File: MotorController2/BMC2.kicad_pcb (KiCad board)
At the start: 2 copper layers, 142.2 x 57.2 mm, 132 parts, among them P1 Sensor, P10 GND, P11 I2C, P12 CAN, P2 CAN, P3 DATA, P4 USB_OTG, P5 PhaseA, P6 PhaseB, P7 PhaseC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

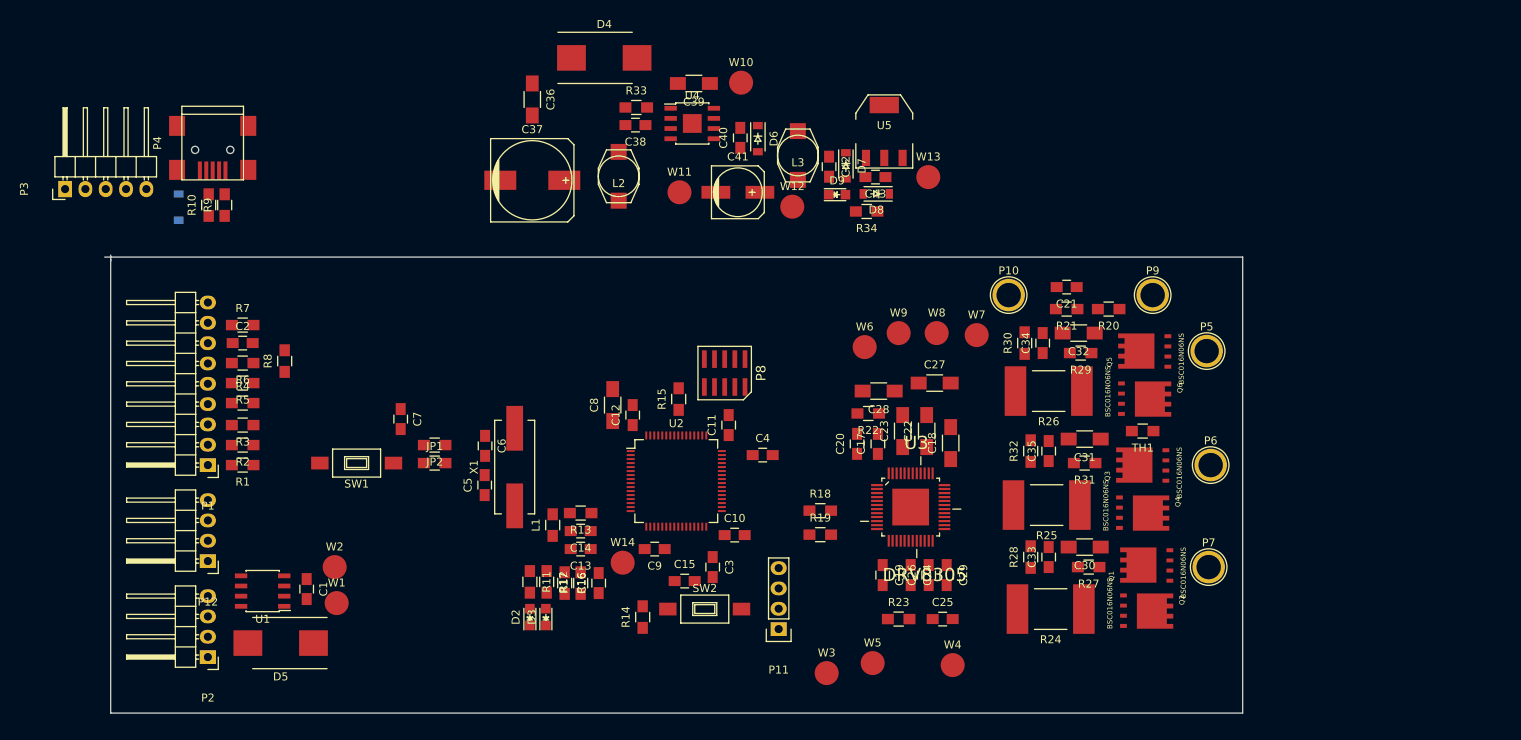
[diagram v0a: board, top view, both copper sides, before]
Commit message: Laying out power section.
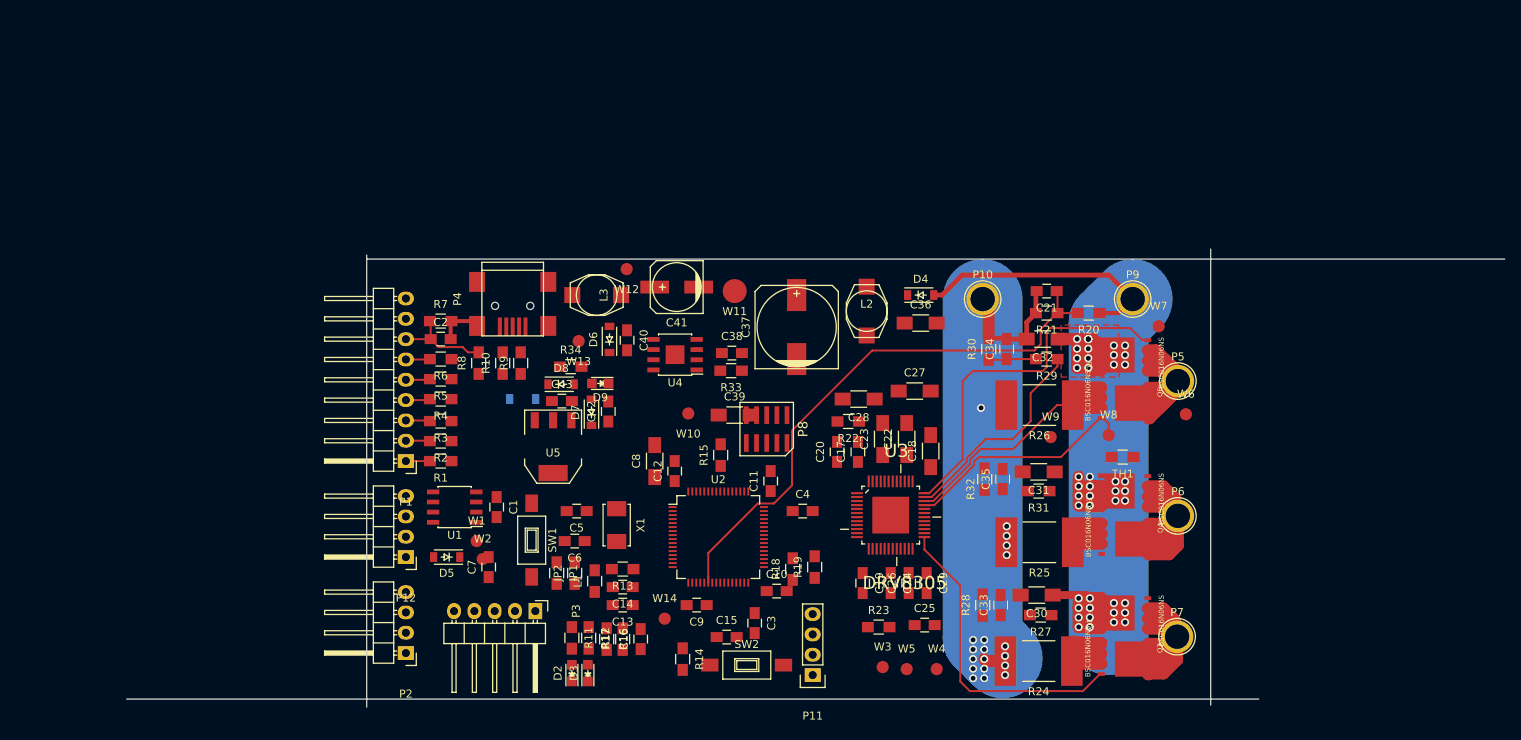
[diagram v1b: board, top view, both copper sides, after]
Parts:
- D4, D5: value D -> 60V 2A; footprint Diodes_SMD:DO-214AB_Handsoldering -> Diodes_SMD:SOD-123
- Q1, Q2, Q3, Q4, Q5, Q6: footprint SON127P532X615X110-8N:SON127P532X615X110-8N -> Local:SON127P532X615X110-8N
- W1, W10, W12, W13, W14, W2, W3, W4, W5, W6, W7, W8, W9: footprint Measurement_Points:Measurement_Point_Round-SMD-Pad_Big -> Measurement_Points:Measurement_Point_Round-SMD-Pad_Small
- X1: footprint Crystals:Crystal_HC49-SD_SMD -> Crystals:ABM3
- moved P3 79.0 mm to (141.1, 99.0), turned to 270 degrees
- moved U5 57.2 mm to (143.3, 78.5), turned to 180 degrees
- moved C36 56.0 mm to (189.2, 63.0), turned to 0 degrees
- moved D4 49.4 mm to (189.2, 59.5)
- moved D1 49.2 mm to (139.5, 72.5), turned to 180 degrees
- moved W13 48.3 mm to (146.5, 65.2), turned to 180 degrees
- moved C43 48.2 mm to (144.4, 72.8), turned to 0 degrees
- moved D8 46.0 mm to (144.3, 70.7), turned to 0 degrees
- moved D7 44.3 mm to (148.1, 74.2), turned to 90 degrees
- moved P4 42.3 mm to (138.2, 60.0)
- moved R9 41.9 mm to (139.2, 68.0)
- moved W10 41.9 mm to (160.2, 74.3), turned to 180 degrees
- moved R34 41.8 mm to (145.5, 68.5), turned to 0 degrees
- moved C39 41.8 mm to (166.0, 74.5), turned to 0 degrees
- moved R10 41.7 mm to (137.0, 68.0)
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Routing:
- net +36V: track 0.00 -> 128.3 mm, vias 0 -> 44
- net GND: track 0.00 -> 76.8 mm, vias 0 -> 19
- net /Controller/VSenseSupply: track 0.00 -> 70.2 mm
- net /power/PhaseA: track 0.00 -> 68.3 mm
- net Net-(Q5-Pad4): track 0.00 -> 45.5 mm
- net Net-(Q2-Pad4): track 0.00 -> 38.9 mm
- net /power/PhaseB: track 0.00 -> 38.8 mm
- net Net-(C29-Pad1): track 0.00 -> 38.5 mm
- net /power/PhaseC: track 0.00 -> 36.7 mm
- net Net-(Q6-Pad4): track 0.00 -> 29.5 mm
- net Net-(C24-Pad1): track 0.00 -> 18.5 mm
- net Net-(C26-Pad1): track 0.00 -> 14.0 mm
- net Net-(C2-Pad1): track 0.00 -> 12.1 mm
- net /Controller/VSenseA: track 0.00 -> 5.69 mm
- net Net-(P1-Pad4): track 0.00 -> 3.05 mm
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- added copper zone on F.Cu, net +36V
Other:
- board size 142.2 x 57.2 mm -> 172.2 x 57.2 mm
- net class Drive added: clearance 0.2, trace_width 0.3, via_dia 0.6, via_drill 0.4
- net class High Power added: clearance 0.2, trace_width 0.25, via_dia 1, via_drill 0.6
- net class Low Power added: clearance 0.2, trace_width 0.5, via_dia 0.6, via_drill 0.4

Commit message: More of the layout done.
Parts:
- removed W6: SHA, Measurement_Points:Measurement_Point_Round-SMD-Pad_Small
- removed W9: SLA, Measurement_Points:Measurement_Point_Round-SMD-Pad_Small
- R24, R25, R26: footprint Local:R_PSR400 -> Local:R_PSR400_SENSE
- moved R7 42.4 mm to (138.1, 104.2)
- moved C2 42.4 mm to (138.0, 106.5)
- moved R8 39.9 mm to (142.5, 107.0), turned to 270 degrees
- moved C7 37.5 mm to (165.2, 71.0), turned to 180 degrees
- moved R6 35.6 mm to (138.1, 102.0)
- moved R5 31.1 mm to (138.2, 99.8)
- moved JP1 28.5 mm to (164.2, 74.5)
- moved JP2 28.5 mm to (166.5, 74.5)
- moved R4 26.3 mm to (138.1, 97.2)
- moved P1 25.8 mm to (133.5, 104.6)
- moved P2 25.4 mm to (133.5, 80.3)
- moved P12 25.0 mm to (133.5, 68.8)
- moved W13 23.5 mm to (137.5, 87.0)
- moved R3 21.4 mm to (138.0, 94.8)
- moved W11 19.9 mm to (185.8, 57.0)
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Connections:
- C24 pad 2: GND -> Net-(C24-Pad2)
- C26 pad 2: GND -> Net-(C26-Pad2)
- C29 pad 2: GND -> Net-(C29-Pad2)
- P1 pad 1: Net-(P1-Pad1) -> Net-(C2-Pad1)
- P1 pad 7: Net-(C2-Pad1) -> Net-(P1-Pad7)
- Q2 pad 1: Net-(C24-Pad1) -> Net-(Q2-Pad1)
- Q2 pad 2: Net-(C24-Pad1) -> Net-(Q2-Pad1)
- Q2 pad 3: Net-(C24-Pad1) -> Net-(Q2-Pad1)
- Q4 pad 1: Net-(C26-Pad1) -> Net-(Q4-Pad1)
- Q4 pad 2: Net-(C26-Pad1) -> Net-(Q4-Pad1)
- Q4 pad 3: Net-(C26-Pad1) -> Net-(Q4-Pad1)
- Q6 pad 1: Net-(C29-Pad1) -> Net-(Q6-Pad1)
- Q6 pad 2: Net-(C29-Pad1) -> Net-(Q6-Pad1)
- Q6 pad 3: Net-(C29-Pad1) -> Net-(Q6-Pad1)
- R1 pad 1: /Controller/EndStop1 -> /Controller/Index
- R1 pad 2: Net-(P1-Pad1) -> Net-(P1-Pad7)
- R2 pad 2: Net-(P1-Pad2) -> Net-(P1-Pad6)
- R24 pad 1: Net-(C24-Pad1) -> Net-(Q2-Pad1)
- R24 pad 2: GND -> Net-(C24-Pad1)
- R25 pad 1: Net-(C26-Pad1) -> Net-(Q4-Pad1)
- R25 pad 2: GND -> Net-(C26-Pad1)
- R26 pad 1: Net-(C29-Pad1) -> Net-(Q6-Pad1)
- R26 pad 2: GND -> Net-(C29-Pad1)
- R3 pad 1: /Controller/Index -> /Controller/EndStop1
- R3 pad 2: Net-(P1-Pad3) -> Net-(P1-Pad5)
- R5 pad 2: Net-(P1-Pad5) -> Net-(P1-Pad3)
- R6 pad 2: Net-(P1-Pad6) -> Net-(P1-Pad2)
- U2 pad 34: /Controller/INLA -> /Controller/INLC
- U2 pad 36: /Controller/INLC -> /Controller/INLA
- U2 pad 41: /Controller/INHA -> /Controller/INHC
- U2 pad 43: /Controller/INHC -> /Controller/INHA
- U3 pad 19: GND -> Net-(C24-Pad2)
- U3 pad 21: GND -> Net-(C26-Pad2)
- U3 pad 23: GND -> Net-(C29-Pad2)
- U3 pad 26: Net-(C24-Pad1) -> Net-(Q2-Pad1)
- U3 pad 31: Net-(C26-Pad1) -> Net-(Q4-Pad1)
- U3 pad 34: Net-(C29-Pad1) -> Net-(Q6-Pad1)
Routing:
- net GND: track 76.8 -> 298.7 mm, vias 19 -> 48
- net /Controller/TempDrv: track 0.00 -> 99.0 mm, vias 0 -> 2
- net /Controller/VSenseC: track 0.00 -> 83.0 mm, vias 0 -> 2
- net +36V: track 128.3 -> 204.3 mm, vias 44 -> 46
- net /Controller/VSenseB: track 0.00 -> 57.4 mm, vias 0 -> 2
- net Net-(C29-Pad2): track 0.00 -> 53.4 mm, vias 0 -> 2
- net Net-(Q2-Pad1): track 0.00 -> 50.2 mm
- net /power/PhaseC: track 36.7 -> 76.6 mm
- net Net-(Q6-Pad1): track 0.00 -> 38.5 mm
- net /power/PhaseB: track 38.8 -> 77.3 mm, vias 0 -> 2
- net Net-(Q3-Pad4): track 0.00 -> 37.0 mm
- net Net-(Q4-Pad1): track 0.00 -> 35.9 mm, vias 0 -> 2
- net Net-(C26-Pad2): track 0.00 -> 35.8 mm, vias 0 -> 2
- net Net-(Q1-Pad4): track 0.00 -> 32.3 mm
- net /Controller/VSenseA: track 5.69 -> 37.6 mm
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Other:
- board size 172.2 x 57.2 mm -> 178.2 x 57.8 mm

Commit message: More tweaks
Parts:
- moved C24 0.50 mm to (186.2, 95.6)
- moved R19 0.45 mm to (179.8, 92.8)
- moved C29 0.40 mm to (190.6, 93.1)
- moved C26 0.30 mm to (188.4, 95.1)
- moved C19 0.20 mm to (182.2, 94.6)
- moved R18 0.20 mm to (177.8, 92.8)
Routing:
- net Net-(C24-Pad2): track 29.0 -> 35.2 mm
- net Net-(C24-Pad1): track 31.7 -> 33.4 mm
- net Net-(C26-Pad1): track 34.8 -> 35.6 mm
- net Net-(C26-Pad2): track 35.8 -> 35.1 mm
- net Net-(C19-Pad1): track 5.19 -> 5.79 mm

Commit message: Layout nearly complete.
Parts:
- added C44: 0.1uf (6V min), Capacitors_SMD:C_0805_HandSoldering, F.Cu at (137.5, 83.5)
- D1: moved to F.Cu
- moved D5 53.4 mm to (186.5, 56.5)
- moved W11 43.0 mm to (186.2, 100.0)
- moved W7 26.5 mm to (193.5, 70.5)
- moved W10 16.5 mm to (166.5, 59.2)
- moved R33 14.9 mm to (152.8, 59.0), turned to 0 degrees
- moved D6 14.8 mm to (164.2, 57.8)
- moved L3 13.6 mm to (163.0, 68.5), turned to 0 degrees
- moved C38 12.9 mm to (152.8, 61.2), turned to 180 degrees
- moved W2 11.9 mm to (146.5, 83.5)
- moved C41 11.0 mm to (154.5, 66.2), turned to 0 degrees
- moved C40 10.9 mm to (164.2, 63.2), turned to 90 degrees
- moved U4 7.43 mm to (159.2, 59.5), turned to 0 degrees
- moved W12 5.13 mm to (160.8, 65.0), turned to 0 degrees
- moved SW1 4.09 mm to (146.4, 95.7), turned to 0 degrees
- moved JP1 3.65 mm to (164.2, 78.2), turned to 90 degrees
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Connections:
- U4 pad 9: (no net) -> GND
- U5 pad 4: (no net) -> +3V3
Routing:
- net GND: track 298.6 -> 685.9 mm, vias 48 -> 78
- net +3V3: track 27.0 -> 193.5 mm, vias 0 -> 7
- net +5V: track 0.00 -> 90.2 mm, vias 0 -> 2
- net +8V: track 0.00 -> 72.6 mm, vias 0 -> 1
- net NRST: track 2.15 -> 66.0 mm, vias 0 -> 4
- net /Controller/USB_DP: track 0.00 -> 56.6 mm, vias 0 -> 2
- net /Controller/USB_DM: track 0.00 -> 53.6 mm, vias 0 -> 2
- net Net-(C37-Pad1): track 0.00 -> 39.9 mm
- net /Controller/EndStop1: track 0.00 -> 36.4 mm, vias 0 -> 2
- net /Controller/EndStop2: track 0.00 -> 35.0 mm, vias 0 -> 2
- net /Controller/Index: track 0.00 -> 34.6 mm, vias 0 -> 2
- net +3.3VADC: track 12.3 -> 44.0 mm, vias 0 -> 2
- net /Controller/CAN_RX: track 0.00 -> 30.4 mm, vias 0 -> 2
- net /Controller/CAN_STBY: track 0.00 -> 30.2 mm, vias 0 -> 2
- net /Controller/UART_RX: track 0.00 -> 28.9 mm
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- added copper zone on B.Cu, net +36V
- added copper zone on F.Cu, net /power/PhaseA
- added copper zone on F.Cu, net /power/PhaseB
- added copper zone on F.Cu, net /power/PhaseC
- added copper zone on B.Cu, net GND
- added copper zone on F.Cu, net GND

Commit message: About to change via drill size.
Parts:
- moved W2 7.91 mm to (144.0, 76.0)
- moved R8 3.25 mm to (142.5, 103.8)
- moved W13 1.58 mm to (138.0, 85.5)
- moved W1 1.53 mm to (142.7, 83.2)
- moved C8 1.05 mm to (158.2, 79.2)
- moved D5 0.95 mm to (187.4, 56.8)
- moved C39 0.71 mm to (173.5, 69.8)
- moved X1 0.55 mm to (154.8, 86.2)
- moved SW2 0.55 mm to (170.2, 107.2)
- moved D2 0.50 mm to (159.8, 107.2)
- moved D3 0.50 mm to (162.0, 107.2)
- moved P4 0.50 mm to (141.2, 60.2)
- moved C5 0.41 mm to (151.4, 83.6)
- moved C6 0.40 mm to (151.4, 88.3)
- moved R10 0.35 mm to (136.8, 68.0)
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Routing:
- net GND: track 685.9 -> 719.0 mm, vias 78 -> 81
- net (no net): track 0.00 -> 10.2 mm, vias 1 -> 0
- net Net-(Q3-Pad4): track 36.6 -> 44.6 mm
- net Net-(C37-Pad1): track 39.9 -> 44.2 mm
- net /Controller/Temp: track 28.0 -> 24.2 mm
- net Net-(P4-Pad3): track 6.66 -> 9.73 mm
- net /Controller/CAN_RX: track 30.4 -> 32.8 mm
- net Net-(P12-Pad4): track 21.2 -> 23.1 mm
- net Net-(P4-Pad2): track 5.20 -> 7.12 mm
- net /power/PhaseB: track 94.8 -> 93.2 mm
- net Net-(C2-Pad1): track 12.9 -> 13.9 mm
- net +8V: track 72.6 -> 73.5 mm
- net /Controller/UART_TX: track 27.3 -> 26.4 mm
- net /Controller/USB_DM: track 53.6 -> 54.5 mm
- net /Controller/VSenseC: track 105.4 -> 104.6 mm
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- removed copper zone on F.Cu, net +36V
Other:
- board size 178.2 x 57.8 mm -> 96 x 56 mm
- net class Default: via_drill 0.4 -> 0.3
- net class Drive: via_drill 0.4 -> 0.3
- net class Low Power: via_drill 0.4 -> 0.3

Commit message: Nearly there.
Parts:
- moved R14 2.50 mm to (174.8, 100.1)
- moved C3 2.25 mm to (172.5, 100.0)
- moved C27 1.46 mm to (189.2, 72.8)
- moved W7 1.25 mm to (192.5, 69.8)
- moved C18 1.14 mm to (190.5, 78.0)
- moved R22 0.55 mm to (180.8, 75.3)
- moved C35 0.25 mm to (199.5, 82.2)
- moved R32 0.25 mm to (197.2, 82.2)
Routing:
- net GND: track 719.0 -> 707.8 mm, vias 81 -> 86
- net Net-(Q3-Pad4): track 44.6 -> 36.9 mm
- net /power/PhaseB: track 93.2 -> 99.1 mm
- net Net-(C3-Pad1): track 8.99 -> 5.75 mm
- net Net-(C15-Pad1): track 16.3 -> 19.0 mm
- net /Controller/MISO: track 17.2 -> 15.8 mm
- net Net-(Q5-Pad4): track 47.1 -> 48.4 mm
- net +36V: track 221.6 -> 222.7 mm
- net +3V3: track 193.9 -> 194.9 mm
- net Net-(C27-Pad1): track 13.4 -> 12.4 mm
- net /Controller/VSenseC: track 104.6 -> 105.5 mm
- net /Controller/VSenseSupply: track 70.9 -> 71.6 mm
- net +5V: track 90.1 -> 89.5 mm
- net Net-(Q4-Pad4): track 29.9 -> 30.4 mm

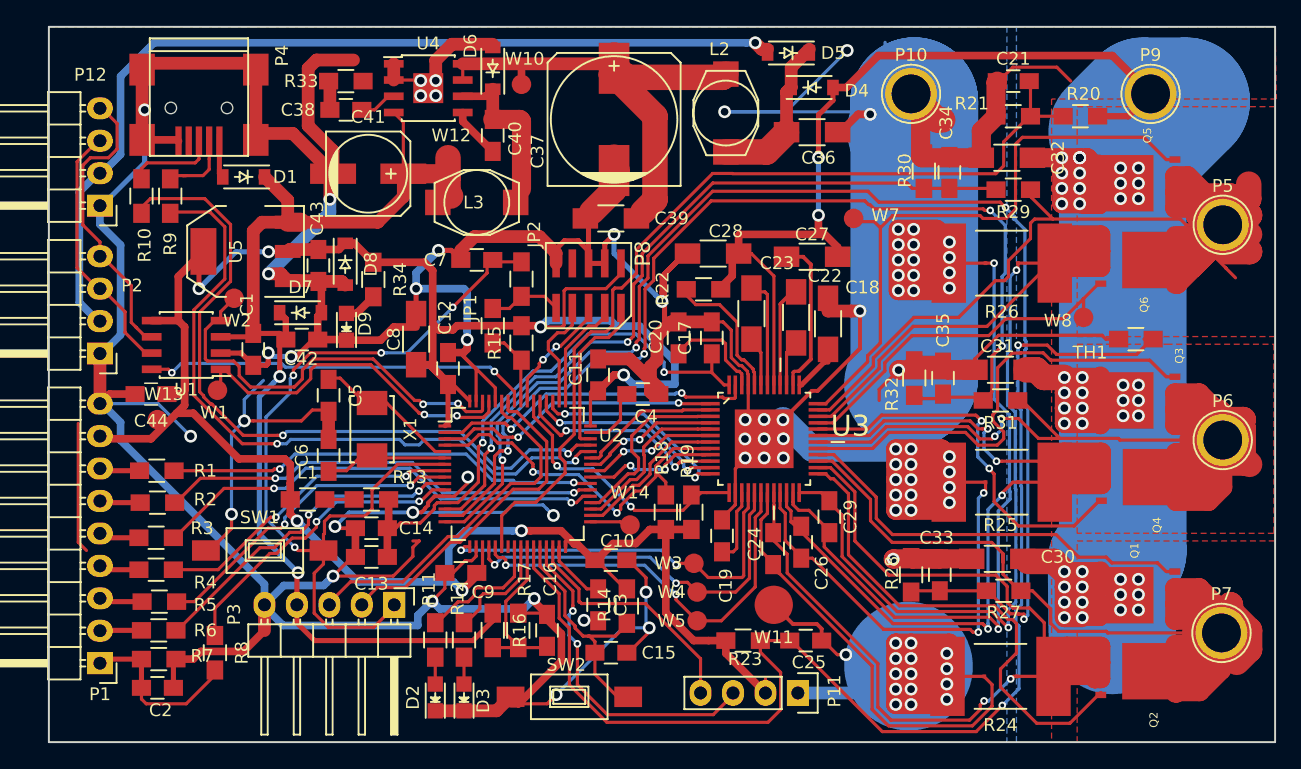
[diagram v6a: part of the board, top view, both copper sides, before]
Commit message: Fixes for soldermask clearences
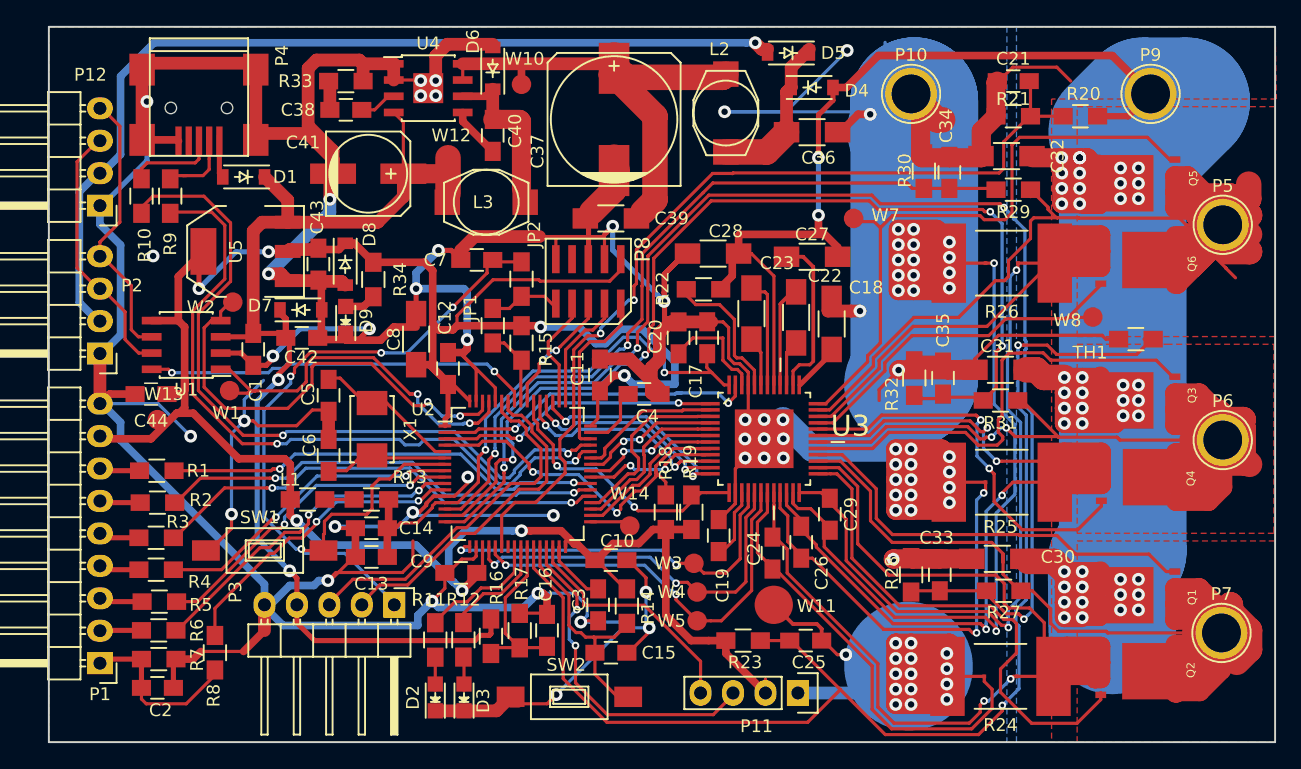
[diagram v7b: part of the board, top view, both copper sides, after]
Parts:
- moved W1 0.95 mm to (143.7, 83.2)
- moved L3 0.74 mm to (163.7, 68.5)
- moved W8 0.73 mm to (211.2, 77.5)
- moved D9 0.55 mm to (152.7, 77.7)
- moved R16 0.48 mm to (164.1, 102.5)
- moved C17 0.36 mm to (181.0, 79.1)
- moved C24 0.35 mm to (186.2, 96.0)
- moved P8 0.33 mm to (171.7, 74.7)
- moved W2 0.32 mm to (143.9, 76.3)
- moved C18 0.28 mm to (190.8, 78.0)
- moved C19 0.26 mm to (181.9, 94.6)
- moved D7 0.23 mm to (149.2, 76.9)
- moved C29 0.19 mm to (190.6, 92.9)
- moved C11 0.14 mm to (172.6, 82.0)
- moved C32 0.13 mm to (204.5, 64.9)
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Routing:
- net GND: track 707.8 -> 723.1 mm
- net +36V: track 222.7 -> 236.4 mm
- net (no net): track 10.2 -> 0.00 mm, vias 0 -> 1
- net +3V3: track 194.9 -> 200.6 mm
- net /power/PhaseA: track 113.8 -> 118.1 mm
- net /Controller/CAN_RX: track 32.8 -> 35.9 mm
- net NRST: track 66.4 -> 63.4 mm
- net /Controller/CAN_TX: track 27.2 -> 29.2 mm
- net Net-(P12-Pad4): track 23.1 -> 21.6 mm
- net /Controller/ISenseA: track 30.6 -> 29.4 mm
- net /power/PhaseB: track 99.1 -> 98.0 mm
- net +5V: track 89.5 -> 88.5 mm
- net /Controller/USB_DP: track 56.7 -> 57.7 mm
- net Net-(Q2-Pad4): track 38.7 -> 39.7 mm
- net Net-(C18-Pad1): track 2.94 -> 3.76 mm
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
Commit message: Work on BOM.
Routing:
- net GND: track 723.1 -> 735.2 mm
- net Net-(Q2-Pad1): track 56.9 -> 53.1 mm
- net /power/PhaseA: track 118.1 -> 121.3 mm
- net Net-(Q4-Pad1): track 39.3 -> 40.0 mm
- net (no net): vias 1 -> 0
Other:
- board text added: "BMC V2.0"
